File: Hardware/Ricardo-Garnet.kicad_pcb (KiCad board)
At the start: 4 copper layers, 38.5 x 80 mm, 193 parts, among them IC3 AP2205-W5-7, IC4 TPS61089RNRR, IC5 ADS131M04IRUKR, J1 RBUS, J2 USB_C_Receptacle_USB2.0, J3 Rotary Pot, J4 Conn_01x02_Male, J5 Conn_01x02_Male, J7 Conn_01x02_Male, J8 Conn_01x02_Male, J9 Conn_01x02_Male, P4 IN+, P5 IN-, P6 MOTOR1, P7 MOTOR2, P9 MOTOR3, Q1 IRFS7530, Q2 IRFS7530, Q3 IRFS7530, Q4 IRFS7530, Q5 IRFS7530, Q6 IRFS7530, U1 ESP32-S3, U10 MAX31856, U11 MAX31856, U3 DRV8302, U4 LM66200DRLR, U5 SC4215, U6 SN65HVD230, U7 MAX77827AEFD+T, U9 THVD2429, Y2 R940000171

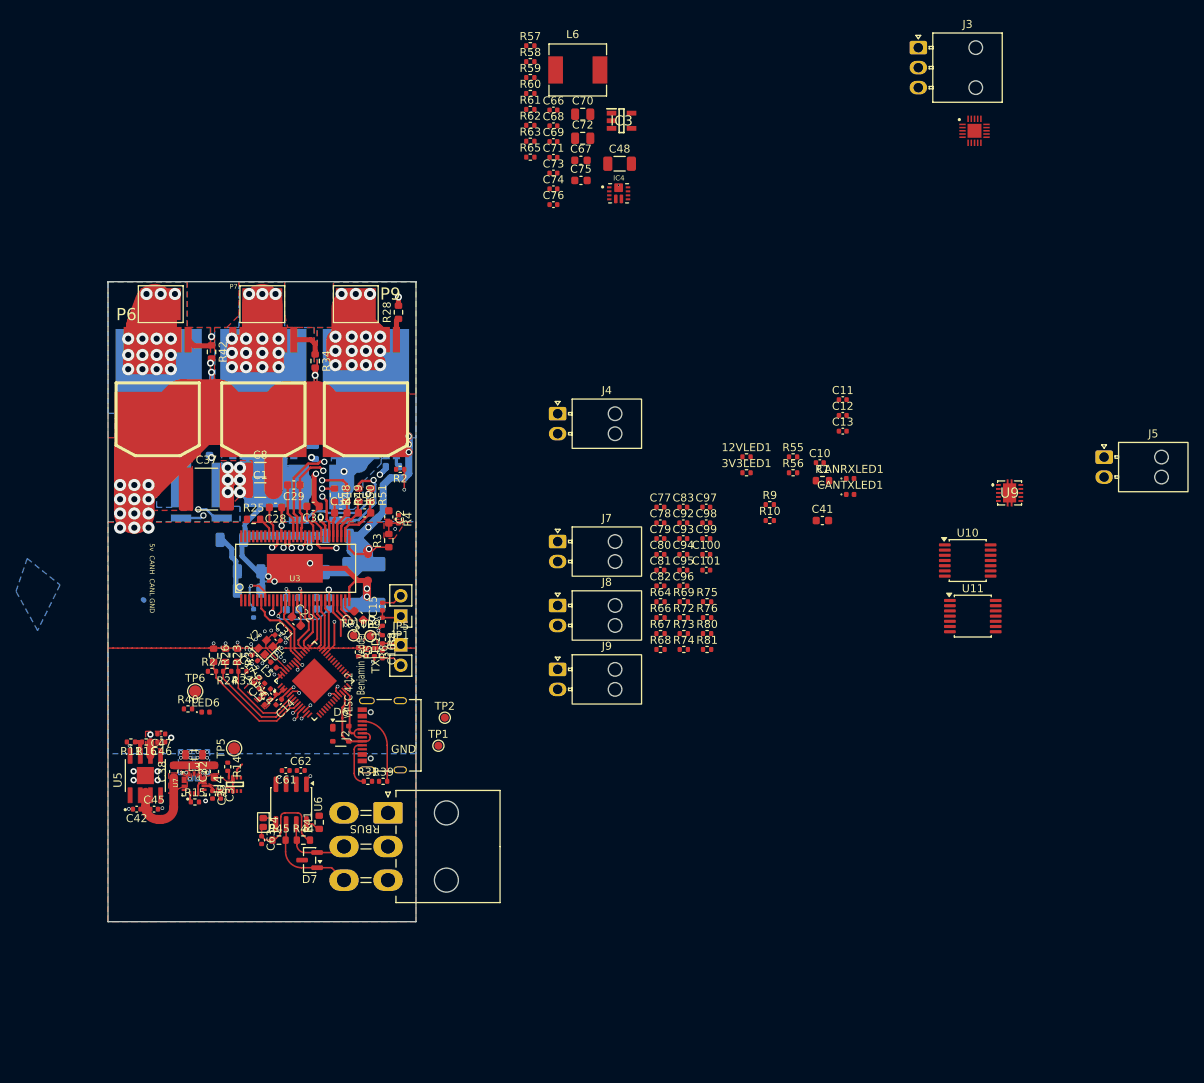
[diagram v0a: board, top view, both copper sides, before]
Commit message: updated settled pcb design
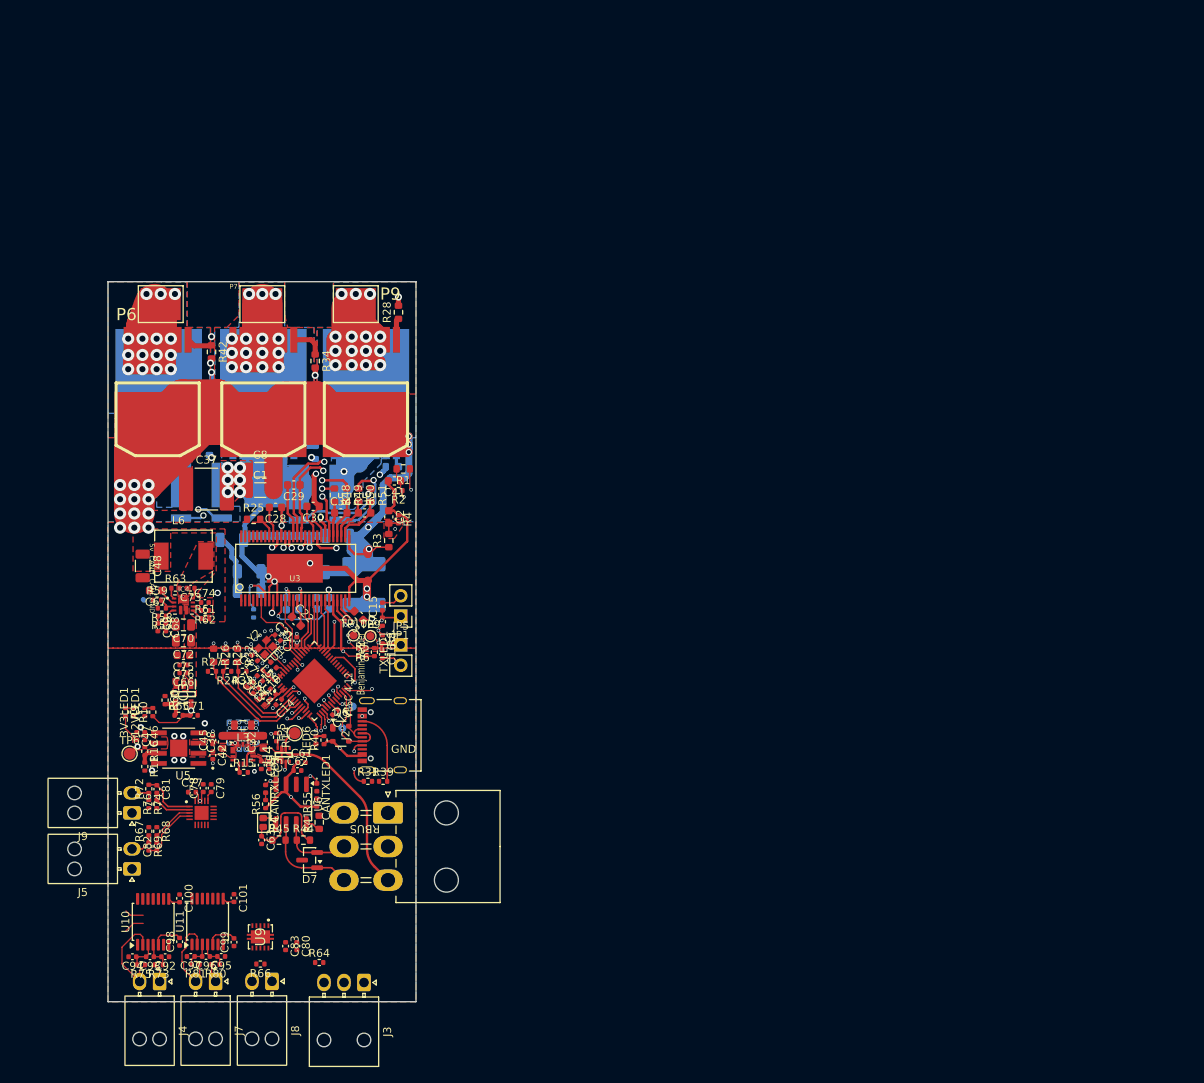
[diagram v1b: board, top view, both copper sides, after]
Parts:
- TP1, TP2: moved to B.Cu
- moved J3 135.9 mm to (110.5, 167.6), turned to -90 degrees
- moved J5 132.0 mm to (81.5, 153.4), turned to 180 degrees
- moved IC5 128.9 mm to (90.2, 146.4)
- moved U10 111.4 mm to (84.1, 160.0), turned to 90 degrees
- moved U9 108.9 mm to (97.5, 161.9), turned to -90 degrees
- moved U11 103.0 mm to (91.0, 160.0), turned to 90 degrees
- moved IC3 90.2 mm to (87.9, 131.5), turned to -90 degrees
- moved R60 88.5 mm to (85.6, 132.3), turned to -90 degrees
- moved J4 86.7 mm to (84.9, 167.5), turned to -90 degrees
- moved C97 85.5 mm to (88.8, 164.3), turned to 180 degrees
- moved C94 85.3 mm to (81.5, 164.4), turned to 180 degrees
- moved R57 84.9 mm to (85.2, 121.8), turned to 180 degrees
- moved C93 84.7 mm to (83.8, 164.4), turned to 180 degrees
- moved R9 84.6 mm to (80.7, 133.8), turned to -90 degrees
- moved C92 84.5 mm to (85.7, 164.4), turned to 180 degrees
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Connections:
- J1 pad 4: DEP -> unconnected-(J1-Pin_4-Pad4)
- R10 pad 1: DEP -> +12V
- R73 pad 2: Net-(J4-Pin_2) -> Net-(J4-Pin_1)
- R75 pad 1: Net-(J4-Pin_1) -> Net-(J4-Pin_2)
- R80 pad 2: Net-(J7-Pin_2) -> Net-(J7-Pin_1)
- R81 pad 1: Net-(J7-Pin_1) -> Net-(J7-Pin_2)
- U10 pad 2: Net-(J4-Pin_1) -> Net-(J4-Pin_2)
- U11 pad 2: Net-(J7-Pin_1) -> Net-(J7-Pin_2)
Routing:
- net VCC: track 11.0 -> 157.8 mm, vias 4 -> 15
- net /MOD_TX: track 0.00 -> 48.4 mm, vias 0 -> 1
- net /TC_CS_0: track 0.00 -> 48.2 mm, vias 0 -> 1
- net /MOD_RX: track 0.00 -> 46.0 mm, vias 0 -> 1
- net /HSPI_MISO: track 0.00 -> 40.6 mm, vias 0 -> 1
- net /MOD_DE: track 0.00 -> 40.3 mm, vias 0 -> 1
- net /HSPI_MOSI: track 0.00 -> 38.1 mm, vias 0 -> 1
- net +12V: track 0.00 -> 37.6 mm, vias 0 -> 1
- net /HSPI_SCLK: track 0.00 -> 36.8 mm, vias 0 -> 1
- net /ACD_CS: track 0.00 -> 33.6 mm, vias 0 -> 1
- net /TC_CS_1: track 0.00 -> 32.1 mm, vias 0 -> 1
- net +5V: track 0.00 -> 25.9 mm, vias 0 -> 4
- net RBUS_uC_V: track 1.93 -> 25.9 mm
- net /ACD_CLK: track 0.00 -> 22.5 mm, vias 0 -> 1
- net GND: track 234.6 -> 256.9 mm, vias 48 -> 53
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- added copper zone on F.Cu, net /Boosts/LDO12.6V_IN
- added copper zone on F.Cu, net Net-(IC4-SW)
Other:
- board size 38.5 x 80 mm -> 38.5 x 90 mm

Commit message: close to 1st done
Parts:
- removed C34, C36: 2.2n, Capacitor_SMD:C_0603_1608Metric
- removed R48, R49, R50, R51: 100R, Resistor_SMD:R_0603_1608Metric
- added C19: 2.2n, Capacitor_SMD:C_0603_1608Metric, F.Cu at (107.6, 108.9)
- added C21: 2.2n, Capacitor_SMD:C_0603_1608Metric, F.Cu at (110.6, 108.9)
- added R12: 100R, Resistor_SMD:R_0603_1608Metric, F.Cu at (106.8, 106.6)
- added R13: 100R, Resistor_SMD:R_0603_1608Metric, F.Cu at (108.3, 106.6)
- added R17: 100R, Resistor_SMD:R_0603_1608Metric, F.Cu at (109.8, 106.6)
- added R18: 100R, Resistor_SMD:R_0603_1608Metric, F.Cu at (111.3, 106.6)
- C2, R3, R4: moved to B.Cu
- C43, C44, C49, R20: moved to F.Cu
- RXD: renamed from TP10; moved to B.Cu
- TXD: renamed from TP9; moved to B.Cu
- moved C43 18.1 mm to (112.0, 111.7)
- moved C80 17.4 mm to (85.7, 157.3)
- moved C49 16.1 mm to (112.0, 116.3)
- moved C44 16.0 mm to (112.0, 114.0)
- moved J8 15.5 mm to (84.0, 163.9)
- moved U9 15.5 mm to (82.5, 158.3)
- moved C83 15.4 mm to (85.7, 159.5)
- moved R66 15.2 mm to (82.8, 161.7)
- moved R30 10.5 mm to (112.2, 103.2), turned to 0 degrees
- moved RXD 7.97 mm to (101.5, 126.2), turned to 180 degrees
- moved LOGIC 7.45 mm to (107.1, 141.7)
- moved C96 6.94 mm to (96.7, 160.8)
- moved C97 6.94 mm to (94.8, 160.8)
- moved C98 6.94 mm to (93.4, 158.9)
- moved C99 6.94 mm to (100.2, 159.0)
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- renumbered 12VLED1 to 12V, 3V3LED1 to 3V3, CANRXLED1 to CANRX, CANTXLED1 to CANTX, TP2 to Dat+, TP1 to Dat-, TP5 to LOGIC, TXLED1 to TX, TP6 to VCC
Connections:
- net /Mosfet driver/H1_VS renamed /Mosfet driver/SH_A
- net /Mosfet driver/H2_VS renamed /Mosfet driver/SH_B
- net /Mosfet driver/H3_VS renamed /Mosfet driver/SH_C
- net /Mosfet driver/M_H1 renamed /Mosfet driver/GH_A
- net /Mosfet driver/M_H2 renamed /Mosfet driver/GH_B
- net /Mosfet driver/M_H3 renamed /Mosfet driver/GH_C
- net /Mosfet driver/M_L1 renamed /Mosfet driver/GL_A
- net /Mosfet driver/M_L2 renamed /Mosfet driver/GL_B
- net /Mosfet driver/M_L3 renamed /Mosfet driver/GL_C
- Q2 pad S: GND -> /Mosfet driver/SL_A
- Q6 pad S: GND -> /Mosfet driver/SL_C
- R30 pad 1: GND -> /Mosfet driver/SL_A
- R46 pad 1: GND -> /Mosfet driver/SL_C
- R53 pad 2: GND -> /Mosfet driver/SL_A
- R53 pad 3: /Mosfet driver/SH2_B -> Net-(R18-Pad1)
- R53 pad 4: /Mosfet driver/SH2_A -> Net-(R17-Pad1)
- R54 pad 1: GND -> /Mosfet driver/SL_C
- R54 pad 3: /Mosfet driver/SH1_A -> Net-(R12-Pad1)
- R54 pad 4: /Mosfet driver/SH1_B -> Net-(R13-Pad1)
- U1 pad 10: /BR_SO2 -> /SENS1
- U1 pad 11: /BR_SO1 -> /SENS2
- U1 pad 12: /AN_IN -> /ACD_CLK
- U1 pad 13: /MOS_TEMP -> /MOD_TX
- U1 pad 14: /HSPI_MISO -> /MOD_RX
- U1 pad 15: /HSPI_MOSI -> /HSPI_MISO
- U1 pad 16: /HSPI_SCLK -> /HSPI_MOSI
- U1 pad 17: /ACD_CLK -> /HSPI_SCLK
- U1 pad 18: /MOD_RX -> /AN_IN
- U1 pad 19: /MOD_TX -> /MOS_TEMP
- U1 pad 21: /TC_CS_0 -> /ACD_CS
- U1 pad 22: /TC_CS_1 -> /TC_CS_0
- U1 pad 27: /MOD_DE -> /TC_CS_1
- U1 pad 36: /ACD_CS -> /MOD_DE
- U1 pad 6: /SENS3 -> /BR_SO1
- U1 pad 7: /SENS1 -> /BR_SO2
- U1 pad 9: /SENS2 -> /SENS3
- U3 pad 30: Net-(U3-SP2) -> /Mosfet driver/SP2
- U3 pad 31: Net-(U3-SN2) -> /Mosfet driver/SN2
- U3 pad 32: Net-(U3-SP1) -> /Mosfet driver/SP1
- U3 pad 33: Net-(U3-SN1) -> /Mosfet driver/SN1
- U3 pad 34: GND -> /Mosfet driver/SL_C
- U3 pad 44: GND -> /Mosfet driver/SL_A
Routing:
- net V_SUPPLY: track 250.6 -> 60.7 mm, vias 17 -> 16
- net GND: track 256.9 -> 70.2 mm, vias 53 -> 54
- net VCC: track 157.8 -> 64.9 mm, vias 15 -> 17
- net /Mosfet driver/SH_B: track 171.3 -> 86.8 mm, vias 17 -> 18
- net /Mosfet driver/SH_A: track 160.4 -> 86.4 mm
- net /Mosfet driver/SH_C: track 157.0 -> 85.7 mm, vias 18 -> 19
- net /Mosfet driver/SL_C: track 0.00 -> 33.4 mm, vias 0 -> 2
- net /Mosfet driver/SL_A: track 0.00 -> 25.9 mm, vias 0 -> 2
- net Net-(R12-Pad1): track 0.00 -> 25.2 mm, vias 0 -> 2
- net /Mosfet driver/SH1_B: track 25.0 -> 0.00 mm, vias 2 -> 0
- net /Mosfet driver/SH1_A: track 24.0 -> 0.00 mm, vias 2 -> 0
- net Net-(R13-Pad1): track 0.00 -> 19.2 mm, vias 0 -> 2
- net /TC_CS_0: track 48.2 -> 31.2 mm, vias 1 -> 2
- net /MOD_TX: track 48.4 -> 32.4 mm, vias 1 -> 2
- net /MOD_RX: track 46.0 -> 31.3 mm, vias 1 -> 2
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- added copper zone on B.Cu, net /AN_IN
- added copper zone on B.Cu, net /Mosfet driver/SL_A
- added copper zone on B.Cu, net /Mosfet driver/SL_C
- added copper zone on In2.Cu, net VCC
- added copper zone on B.Cu, net V_SUPPLY
- removed copper zone on F.Cu, net /AN_IN
- removed copper zone on F.Cu, net /TXD
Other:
- board text added: "5V"
- board text removed: "3.3V"
- board text removed: "3.3v"
- board text removed: "5v"
- board text removed: "ADC"
- board text removed: "ADC2"
- board text removed: "Benjamin Vedder"
- board text removed: "CANH"
- board text removed: "CANL"
- board text removed: "CLK"
- board text removed: "DIO"
- board text removed: "GND"
- board text removed: "H1"
- board text removed: "H2"
- board text removed: "H3"
- board text removed: "MISO"
- board text removed: "MOSI"
- board text removed: "NSS"
- board text removed: "RST"
- board text removed: "RX"
- board text removed: "SCK"
- board text removed: "SCL"
- board text removed: "SDA"
- board text removed: "TEMP"
- board text removed: "TX"
- board text removed: "VESC 4.12"
- board text removed: "vedder.se"

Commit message: final touches and adding encoder
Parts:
- removed R64: 8.56k, Resistor_SMD:R_0402_1005Metric
- added C24: 10u,50V, Capacitor_SMD:C_1206_3216Metric, B.Cu at (82.0, 117.5)
- added C25: 10u,50V, Capacitor_SMD:C_1206_3216Metric, B.Cu at (82.0, 115.2)
- added C27: 15u, 100v, Capacitor_SMD:C_2220_5750Metric, B.Cu at (82.7, 122.3)
- added C33: 10u,50V, Capacitor_SMD:C_1206_3216Metric, B.Cu at (88.1, 120.1)
- added C34: 10u,50V, Capacitor_SMD:C_1206_3216Metric, B.Cu at (88.8, 117.8)
- added C36: 15u, 100v, Capacitor_SMD:C_2220_5750Metric, B.Cu at (89.5, 113.7)
- J3: value Rotary Pot -> 3x2 Nanofit; footprint iclr:Molex_Nano-Fit_105313-xx03_1x03_P2.50mm_Horizontal -> iclr:1053141206
- moved J3 2.37 mm to (107.9, 161.5), turned to 0 degrees
- moved R20 2.00 mm to (95.3, 121.4), turned to 0 degrees
- moved C99 0.38 mm to (100.2, 158.6)
- moved C11 0.10 mm to (107.2, 134.3)
- renumbered 12V to 12VLED1, 3V3 to 3V3LED1, CANRX to CANRXLED1, CANTX to CANTXLED1, Dat- to TP1, RXD to TP10, Dat+ to TP2, LOGIC to TP5, VCC to TP6, TXD to TP9, TX to TXLED1
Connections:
- IC5 pad 5: /sensors/AIN2P -> unconnected-(IC5-AIN2P-Pad5)
- IC5 pad 6: GND -> unconnected-(IC5-AIN2N-Pad6)
- J3 pad 1: GND -> /HSPI_SCLK
- J3 pad 2: /sensors/AIN2P -> /HSPI_MISO
- J3 pad 3: Net-(J3-Pin_3) -> /HSPI_MOSI
- U1 pad 37: unconnected-(U1-SPICLK_P/GPIO47-Pad37) -> /ENCODER_CS
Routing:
- net /ENCODER_CS: track 0.00 -> 49.0 mm, vias 0 -> 1
- net V_SUPPLY: track 60.7 -> 81.5 mm
- net /HSPI_SCLK: track 38.6 -> 52.1 mm
- net /Mosfet driver/SH_C: track 85.7 -> 98.0 mm
- net /HSPI_MISO: track 38.0 -> 50.0 mm
- net /HSPI_MOSI: track 40.0 -> 51.8 mm
- net /Mosfet driver/SH_B: track 86.8 -> 97.9 mm
- net Net-(U3-DTC): track 5.55 -> 7.78 mm
- net /Boosts/LDO12.6V_IN: track 10.2 -> 12.1 mm
- net /Mosfet driver/GH_C: track 38.8 -> 37.8 mm
- net Net-(CANTXLED1-A): track 0.00 -> 0.91 mm
- net VCC: track 64.9 -> 65.8 mm, vias 17 -> 20
- net /Mosfet driver/GL_B: track 18.7 -> 18.0 mm
- net /Mosfet driver/GH_A: track 49.2 -> 48.5 mm
- net GND: track 70.2 -> 70.8 mm, vias 54 -> 103
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
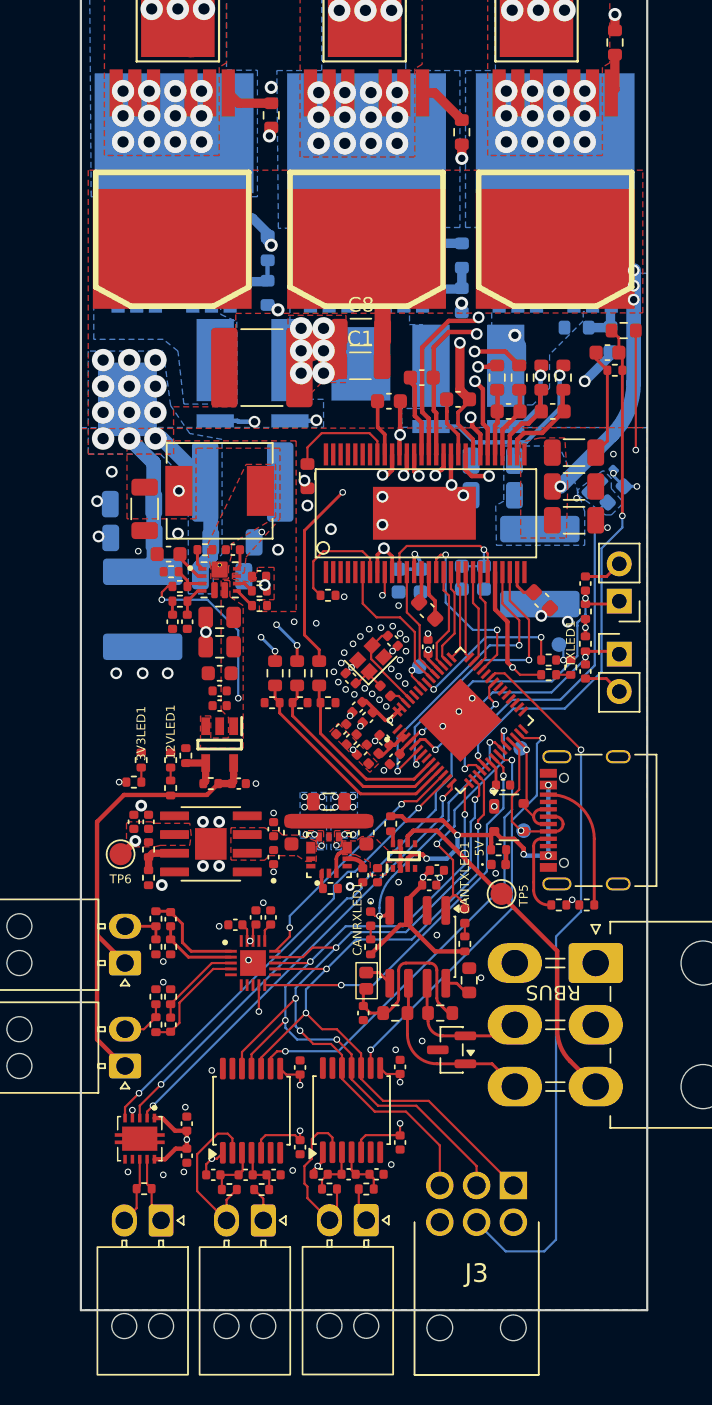
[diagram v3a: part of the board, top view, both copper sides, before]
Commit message: removed some decoupling caps from sims
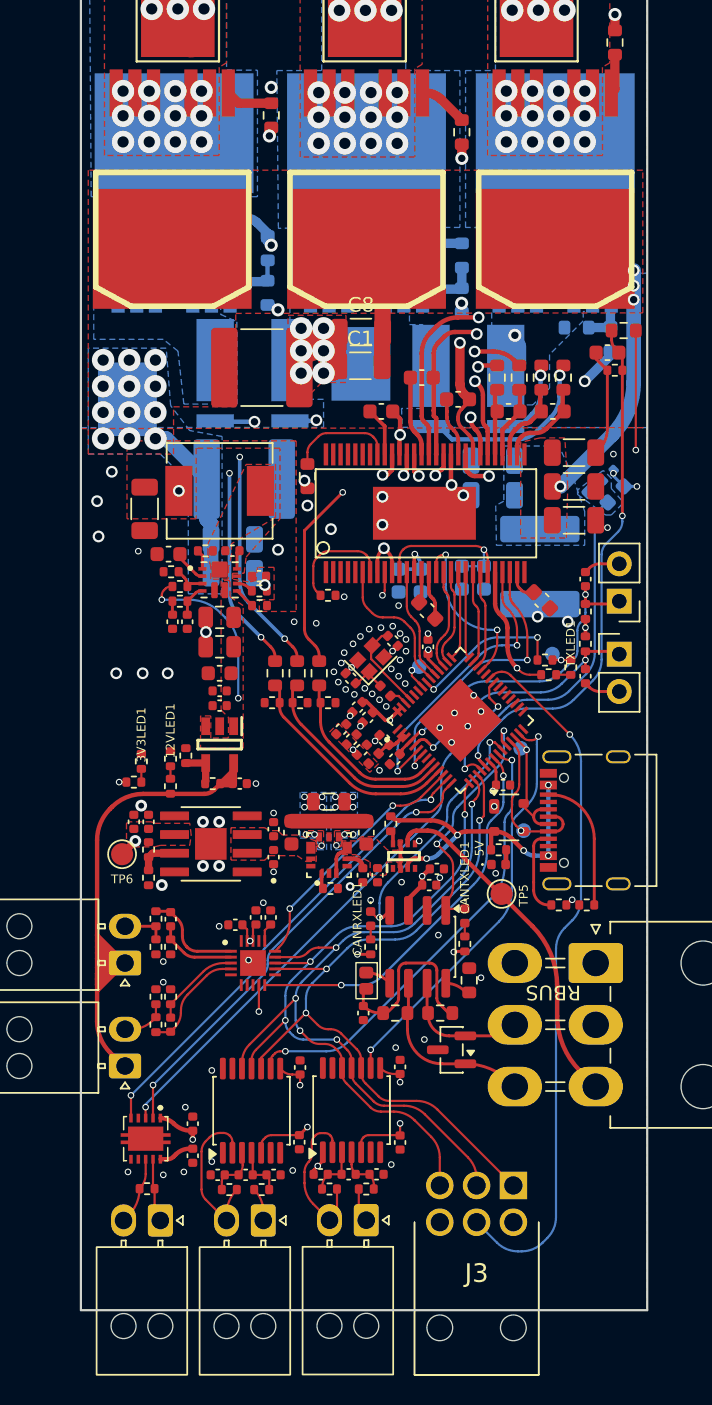
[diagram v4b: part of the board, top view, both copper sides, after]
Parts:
- removed C33, C34: 10u,50V, Capacitor_SMD:C_1206_3216Metric
- removed C36: 15u, 100v, Capacitor_SMD:C_2220_5750Metric
- moved C27 11.2 mm to (89.6, 113.5), turned to 180 degrees
- moved C25 7.26 mm to (88.8, 117.6), turned to 180 degrees
- moved C24 7.23 mm to (88.8, 119.9), turned to 180 degrees
- moved C28 0.87 mm to (98.9, 108.9)
- moved TP9 0.79 mm to (110.5, 125.4)
- moved C80 0.40 mm to (86.1, 157.3)
- moved C83 0.40 mm to (86.1, 159.5)
- moved U9 0.40 mm to (82.9, 158.3)
- moved C98 0.34 mm to (93.3, 158.6)
- moved C16 0.32 mm to (112.8, 126.9)
- moved C15 0.30 mm to (112.8, 120.3)
- moved C94 0.30 mm to (87.8, 160.8)
- moved R6 0.25 mm to (110.0, 125.8)
- moved R66 0.20 mm to (83.0, 161.7)
- moved R65 0.13 mm to (87.5, 134.2)
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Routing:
- net +12V: track 31.8 -> 50.9 mm
- net V_SUPPLY: track 81.5 -> 71.1 mm
- net VCC: track 65.8 -> 56.9 mm, vias 20 -> 21
- net GND: track 70.8 -> 67.5 mm, vias 103 -> 104
- net +5V: track 23.9 -> 22.3 mm
- net /HSPI_MOSI: track 51.8 -> 50.7 mm
- net /HSPI_SCLK: track 52.1 -> 51.2 mm
- net /HSPI_MISO: track 50.0 -> 49.0 mm
- net /ENCODER_CS: track 49.0 -> 48.2 mm
- net /Mosfet driver/SH_B: track 97.9 -> 97.2 mm
- net /AN_IN: track 25.5 -> 25.0 mm
- net /BR_SO1: track 20.6 -> 20.1 mm
- net RBUS_uC_V: track 24.4 -> 23.9 mm
- net /MOS_TEMP: track 36.3 -> 35.8 mm

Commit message: mounting holes looking rough
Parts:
- added H1: MountingHole_Pad, MountingHole:MountingHole_3.2mm_M3_DIN965_Pad, F.Cu at (82.2, 127.0)
- added H2: MountingHole_Pad, MountingHole:MountingHole_3.2mm_M3_DIN965_Pad, F.Cu at (137.5, 164.4)
- added H3: MountingHole_Pad, MountingHole:MountingHole_3.2mm_M3_DIN965_Pad, F.Cu at (137.5, 171.6)
- added H4: MountingHole_Pad, MountingHole:MountingHole_3.2mm_M3_DIN965_Pad, F.Cu at (113.7, 166.7)
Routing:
- net /Mosfet driver/SH_A: track 85.8 -> 84.1 mm
- net /Mosfet driver/SH_B: track 97.2 -> 95.6 mm
- net GND: vias 104 -> 103
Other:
- outline, holes or cut-outs redrawn
